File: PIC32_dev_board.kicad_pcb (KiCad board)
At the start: 2 copper layers, 45.5 x 16.5 mm, 3 parts, among them J1 Conn_01x24_Pin, J2 Conn_01x24_Pin, U2 PIC32CX1012BZ25048

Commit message: still working on routing
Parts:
- moved U2 19.0 mm to (191.6, 55.0)
- moved J2 5.00 mm to (165.5, 44.0)
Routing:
- net Net-(J2-Pin_20): track 24.7 -> 0.08 mm, vias 1 -> 0
- net Net-(J2-Pin_5): track 19.5 -> 1.95 mm, vias 1 -> 0
- net Net-(J1-Pin_24): track 15.9 -> 0.09 mm
- net Net-(J2-Pin_1): track 13.5 -> 0.00 mm, vias 1 -> 0
- net Net-(J2-Pin_18): track 13.1 -> 0.00 mm
- net Net-(J1-Pin_20): track 11.1 -> 1.02 mm
- net Net-(J2-Pin_3): track 11.8 -> 2.06 mm, vias 2 -> 0
- net Net-(J2-Pin_22): track 13.7 -> 4.43 mm
- net Net-(J2-Pin_21): track 13.3 -> 4.22 mm
- net Net-(J1-Pin_19): track 9.87 -> 1.02 mm
- net Net-(J1-Pin_18): track 8.68 -> 1.02 mm
- net Net-(J1-Pin_17): track 7.68 -> 1.02 mm
- net Net-(J2-Pin_12): track 0.00 -> 6.10 mm
- net Net-(J1-Pin_16): track 6.80 -> 1.02 mm
- net Net-(J2-Pin_14): track 0.00 -> 5.39 mm
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- removed copper zone on B.Cu, net unconnected-(U2-GND-Pad49)
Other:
- board size 45.5 x 16.5 mm -> 45.5 x 20.5 mm

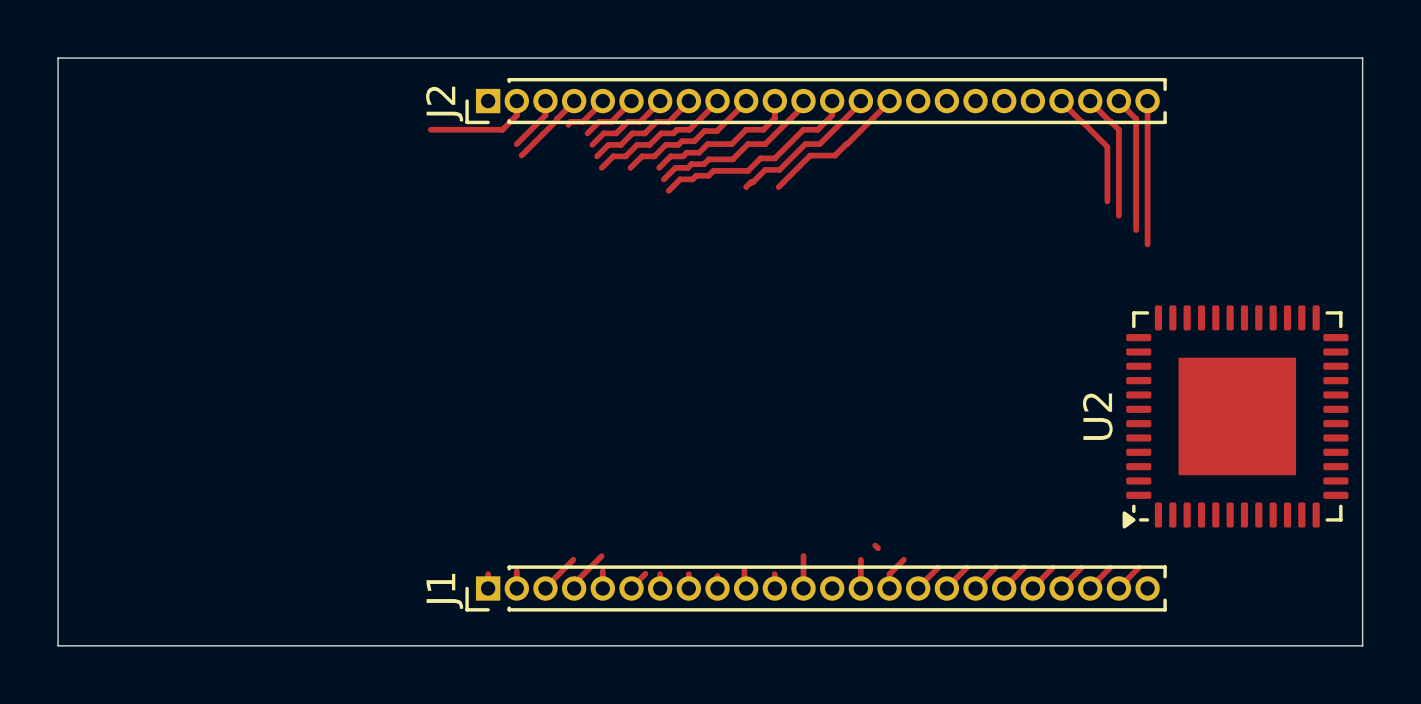
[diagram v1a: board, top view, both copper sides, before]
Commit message: routed breakout board
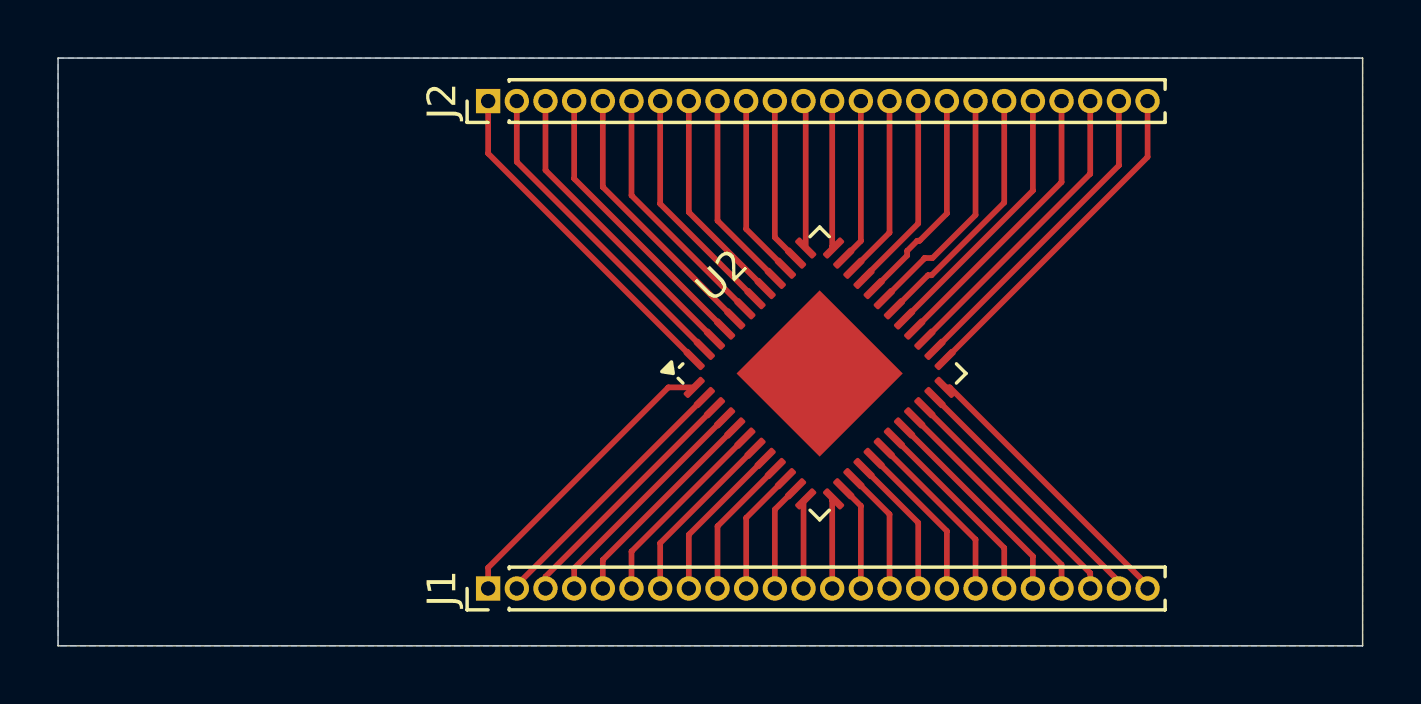
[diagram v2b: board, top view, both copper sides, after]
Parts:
- moved U2 14.6 mm to (177.1, 53.5), turned to 45 degrees
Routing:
- net Net-(J2-Pin_1): track 0.00 -> 12.0 mm
- net Net-(J1-Pin_1): track 0.50 -> 10.5 mm
- net Net-(J1-Pin_24): track 0.09 -> 10.0 mm
- net Net-(J2-Pin_20): track 0.08 -> 9.45 mm
- net Net-(J2-Pin_19): track 0.15 -> 8.91 mm
- net Net-(J1-Pin_2): track 0.62 -> 9.37 mm
- net Net-(J2-Pin_3): track 2.06 -> 10.7 mm
- net Net-(J2-Pin_18): track 0.00 -> 8.38 mm
- net Net-(J1-Pin_23): track 1.02 -> 9.32 mm
- net Net-(J1-Pin_22): track 1.02 -> 8.70 mm
- net Net-(J2-Pin_17): track 0.05 -> 7.64 mm
- net Net-(J2-Pin_5): track 1.95 -> 9.51 mm
- net Net-(J2-Pin_2): track 3.85 -> 11.4 mm
- net Net-(J2-Pin_4): track 2.82 -> 10.1 mm
- net Net-(J1-Pin_3): track 1.51 -> 8.75 mm
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- added copper zone on B.Cu, net unconnected-(U2-GND-Pad49)
